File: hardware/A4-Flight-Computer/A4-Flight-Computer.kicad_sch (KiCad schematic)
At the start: 0 parts

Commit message: add most of A3 components
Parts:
- added BZ1: Buzzer, Buzzer_Beeper:Buzzer_Murata_PKMCS0909E, symbol Device:Buzzer
- added C1, C2: 2.2uF, Capacitor_SMD:C_0402_1005Metric, symbol Device:C_Small_US
- added C17: 100nF, Capacitor_SMD:C_0402_1005Metric, symbol Device:C_Small_US
- added C25: 4.7nF, Capacitor_SMD:C_0402_1005Metric, symbol Device:C_Small_US
- added D1: PWR, LED_SMD:LED_0805_2012Metric, symbol Device:LED
- added D2: STAT1, LED_SMD:LED_0805_2012Metric, symbol Device:LED
- added D3: STAT2, LED_SMD:LED_0805_2012Metric, symbol Device:LED
- added D4, D6, D7: DSS14U, Diode_SMD:D_SOD-123, symbol Diode:BAV16W
- added D8, D9: SMF54CA, Diode_SMD:D_SMF, symbol Diode:SMAJ54CA
- added J1: Conn_02x20_Odd_Even, LAB_PCB_Standard:LAB_PCB_With_Header, symbol Connector_Generic:Conn_02x20_Odd_Even
- added J2: USB_C_Receptacle_USB2.0_14P, Connector_USB:USB_C_Receptacle_Palconn_UTC16-G, symbol Connector:USB_C_Receptacle_USB2.0_14P
- added J5: DEBUG, Connector_PinHeader_2.54mm:PinHeader_2x04_P2.54mm_Vertical, symbol Connector_Generic:Conn_02x04_Odd_Even
- added Q1: IRLML0030, Package_TO_SOT_SMD:SOT-23, symbol Transistor_FET:IRLML0030
- added R1: 250R, Resistor_SMD:R_0402_1005Metric, symbol Device:R_US
- added R10, R9: 5.1K, Resistor_SMD:R_0402_1005Metric, symbol Device:R_Small_US
- added R13, R14: 60, Resistor_SMD:R_0402_1005Metric, symbol Device:R_Small_US
- added R2, R3: 240R, Resistor_SMD:R_0402_1005Metric, symbol Device:R_US
- added R4: 100, Resistor_SMD:R_0402_1005Metric, symbol Device:R_Small_US
- added R5: 100k, Resistor_SMD:R_0402_1005Metric, symbol Device:R_Small_US
- added R6: 10k, Resistor_SMD:R_0402_1005Metric, symbol Device:R_Small_US
- added R7, R8: 27R, Resistor_SMD:R_0402_1005Metric, symbol Device:R_Small_US
- added SW1: RST, Button_Switch_SMD:SW_SPST_TS-1088-xR025, symbol Switch:SW_Push
- added SW2: BOOT, Button_Switch_SMD:SW_SPDT_CK_JS102011SAQN, symbol Switch:SW_SPDT
- added U1: STM32H523RETx, Package_QFP:LQFP-64_10x10mm_P0.5mm, symbol MCU_ST_STM32H5:STM32H523RETx
- added U5: PTCAN3414DR, Package_SO:SOIC-8_5.3x5.3mm_P1.27mm, symbol A3-Flight-Computer-Components:PTCAN3414DR
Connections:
- new net: D3.1 (K), R3.1
- new net: Q1.1 (G), R4.2, R5.2
- new net: BZ1.2 (-), D6.2 (A), Q1.3 (D)
- new net: D2.1 (K), R2.1
- new net: R6.1, SW2.2 (B)
- new net: C25.1, R13.1, R14.2
- new net: C1.1, C2.1, U1.30 (VCAP), U1.62 (VCAP)
- new net: J2.A6 (D+), J2.B6 (D+), R8.2
- new net: J2.A5 (CC1), R9.2
- new net: D7.2 (A), J2.A4 (VBUS), J2.A9 (VBUS), J2.B4 (VBUS), J2.B9 (VBUS)
- new net: D1.1 (K), R1.1
- new net: J2.B5 (CC2), R10.2
- new net: J2.A7 (D-), J2.B7 (D-), R7.2
- new net: D4.2 (A), J1.1 (Pin_1)
- new net +3.3V: BZ1.1 (+), D1.2 (A), D4.1 (K), D6.1 (K), J5.2 (Pin_2), SW2.1 (A), U1.1 (VBAT), U1.13 (VDDA), U1.19 (VDD), U1.32 (VDD), U1.48 (VDD), U1.64 (VDD), U5.3 (VCC)
- new net BOOT: R6.2, U1.60 (BOOT0)
- new net BUZZ: R4.1, U1.24 (PC4)
- new net CAN_H: D8.1 (A1), J1.7 (Pin_7), R13.2, U5.7 (CANH)
- new net CAN_L: D9.2 (A2), J1.9 (Pin_9), R14.1, U5.6 (CANL)
- new net CAN_RX: U1.33 (PB12), U5.4 (RXD)
- new net CAN_SHDN: U1.35 (PB14), U5.5 (SHDN)
- new net CAN_STB: U1.36 (PB15), U5.8 (STB)
- new net CAN_TX: U1.34 (PB13), U5.1 (TXD)
- new net DEBUG_RX: J5.8 (Pin_8), U1.58 (PB6)
- new net DEBUG_TX: J5.7 (Pin_7), U1.57 (PB5)
- new net GND: C1.2, C17.2, C2.2, C25.2, D8.2 (A2), D9.1 (A1), J1.10 (Pin_10), J1.12 (Pin_12), J1.21 (Pin_21), J1.23 (Pin_23), J1.25 (Pin_25), J1.27 (Pin_27), J1.29 (Pin_29), J1.3 (Pin_3), J1.31 (Pin_31), J1.33 (Pin_33), J1.35 (Pin_35), J1.37 (Pin_37), J1.39 (Pin_39), J1.4 (Pin_4), J1.5 (Pin_5), J1.6 (Pin_6), J2.A1 (GND), J2.A12 (GND), J2.B1 (GND), J2.B12 (GND), J2.SH (SHIELD), J5.1 (Pin_1), Q1.2 (S), R1.2, R10.1, R2.2, R3.2, R5.1, R9.1, SW1.1, SW2.3 (C), U1.12 (VSSA), U1.18 (VSS), U1.31 (VSS), U1.47 (VSS), U1.63 (VSS), U5.2 (GND)
- new net GPS_PPS: J1.16 (Pin_16)
- new net JTCK-SWCLK: J5.5 (Pin_5), U1.49 (PA14(JTCK)
- new net JTDI: J5.4 (Pin_4), U1.50 (PA15(JTDI))
- new net JTDO-SWO: J5.3 (Pin_3), U1.55 (PB3(JTDO)
- new net JTMS-SWDIO: J5.6 (Pin_6), U1.46 (PA13(JTMS)
- new net RST: C17.1, SW1.2, U1.7 (NRST)
- new net SEN_SYNC: J1.14 (Pin_14)
- new net STATUS_LED1: D2.2 (A), U1.27 (PB1)
- new net STATUS_LED2: D3.2 (A), U1.28 (PB2)
- new net USB_DM: R7.1, U1.44 (PA11)
- new net USB_DP: R8.1, U1.45 (PA12)
- no-connect marks 0 -> 55
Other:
- note added: "Don't forget, need logic level shifter for SD card if using UHS-I"
- note added: "How many caps between 3v3 and gnd?"
- note added: "^ replace symbol & footprint (copied from A3 library)"
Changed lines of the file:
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@@
 	(generator_version "10.0")
 	(paper "A4")
-	(sheet_instances
-		(path "/"
-			(page "1")
-		)
-	)
-	(embedded_fonts no)
-)

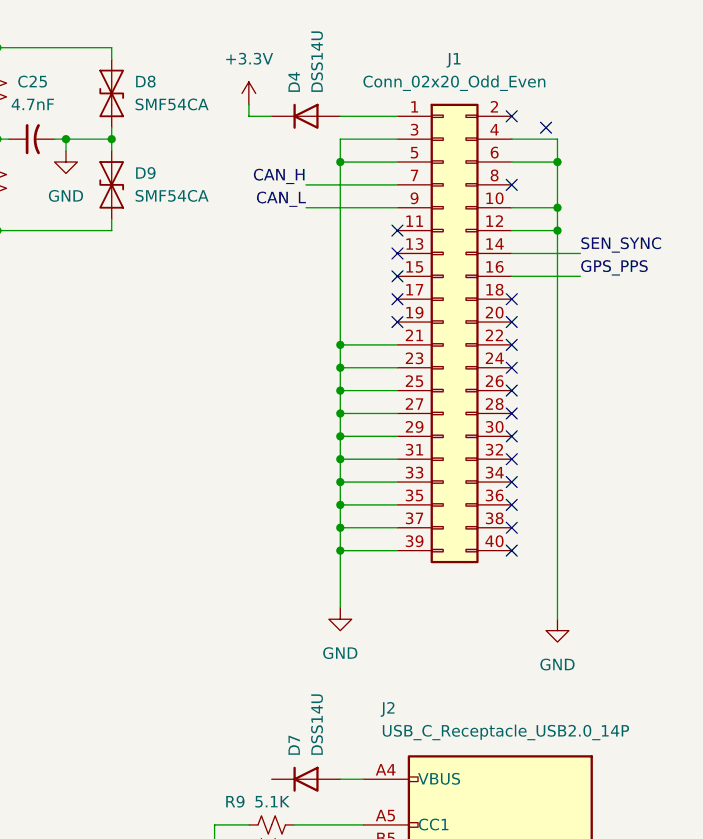
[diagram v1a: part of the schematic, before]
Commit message: add reference to pcb standard footprint/schematic symbols and replace header symbol
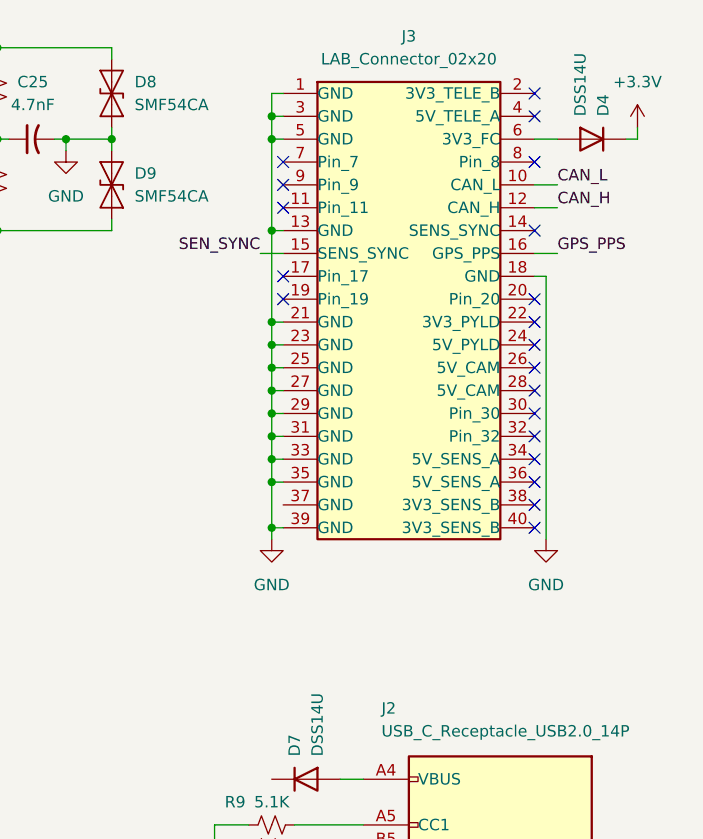
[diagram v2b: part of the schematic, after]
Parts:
- removed J1: Conn_02x20_Odd_Even, LAB_PCB_Standard:LAB_PCB_With_Header, symbol Connector_Generic:Conn_02x20_Odd_Even
- added J3: LAB_Connector_02x20, symbol LAB_PCB_Standard:LAB_Connector_02x20
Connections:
- net CAN_H: now also J3.12 (CAN_H)
- net CAN_L: now also J3.10 (CAN_L)
- net GND: now also J3.1 (GND), J3.13 (GND), J3.18 (GND), J3.21 (GND), J3.23 (GND), J3.25 (GND), J3.27 (GND), J3.29 (GND), J3.3 (GND), J3.31 (GND), J3.33 (GND), J3.35 (GND), J3.39 (GND), J3.5 (GND)
- net GPS_PPS: now also J3.16 (GPS_PPS)
- net SEN_SYNC: now also J3.15 (SENS_SYNC)
- net at D4.2 (A): now also J3.6 (3V3_FC)
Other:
- moved on the sheet: D4

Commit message: update with new pcb standard revision
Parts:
- J3: footprint (none) -> LAB_PCB_Standard:LAB_PCB_With_Header
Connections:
- net CAN_H: now also J3.14 (CAN_H); no longer J3.12 (CAN_H)
- net CAN_L: now also J3.12 (CAN_L); no longer J3.10 (CAN_L)
- net GND: now also J3.10 (GND), J3.2 (GND), J3.26 (GND), J3.34 (GND), J3.37 (GND); no longer J3.1 (GND), J3.23 (GND), J3.25 (GND), J3.27 (GND), J3.3 (GND), J3.31 (GND), J3.33 (GND), J3.35 (GND), J3.39 (GND)
- net at J3.6 (5V_TELE): no longer D4.2 (A)
- net at J3.7 (3V3_FC): now also D4.2 (A)
- no-connect marks 55 -> 60
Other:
- moved on the sheet: C25, D4, D8, D9, R13, R14
